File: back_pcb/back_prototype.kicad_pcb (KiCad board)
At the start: 2 copper layers, 40 x 100 mm, 74 parts, among them P1 EXPANSION_LEFT, P2 EXPANSION_BOTTOM, P3 EXPANSION_TOP, P4 USB_A, P5 AUDIO_CONN, P6 ATMEGA_HEADER, P7 EXPANSION_BOTTOM2, P8 JST, P9 USB_A, Q1 IRLML6401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

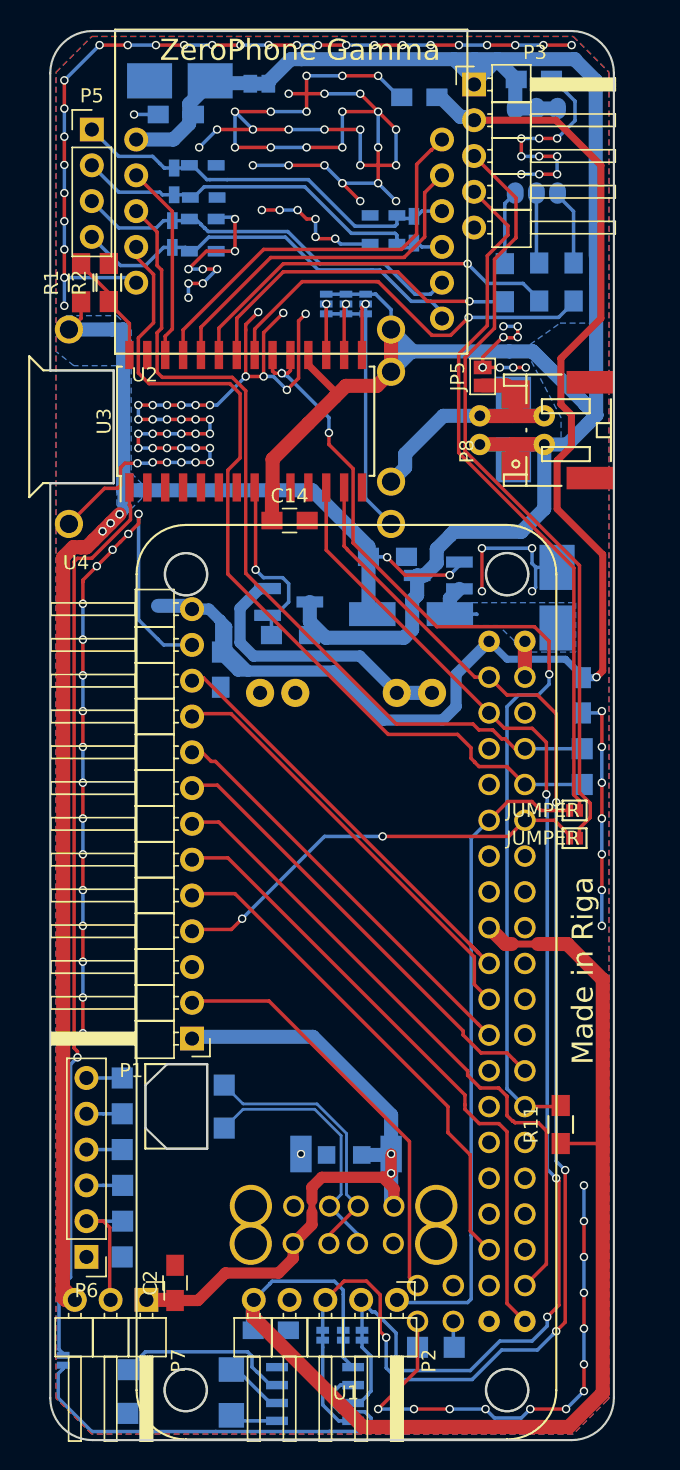
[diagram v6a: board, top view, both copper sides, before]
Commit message: Updated back board
* Added a footprint for MPU9050/9150 breakouts
* Added a FET that interrupts VBAT+ and is controlled from GPIO expander
(with a button to reset it?)
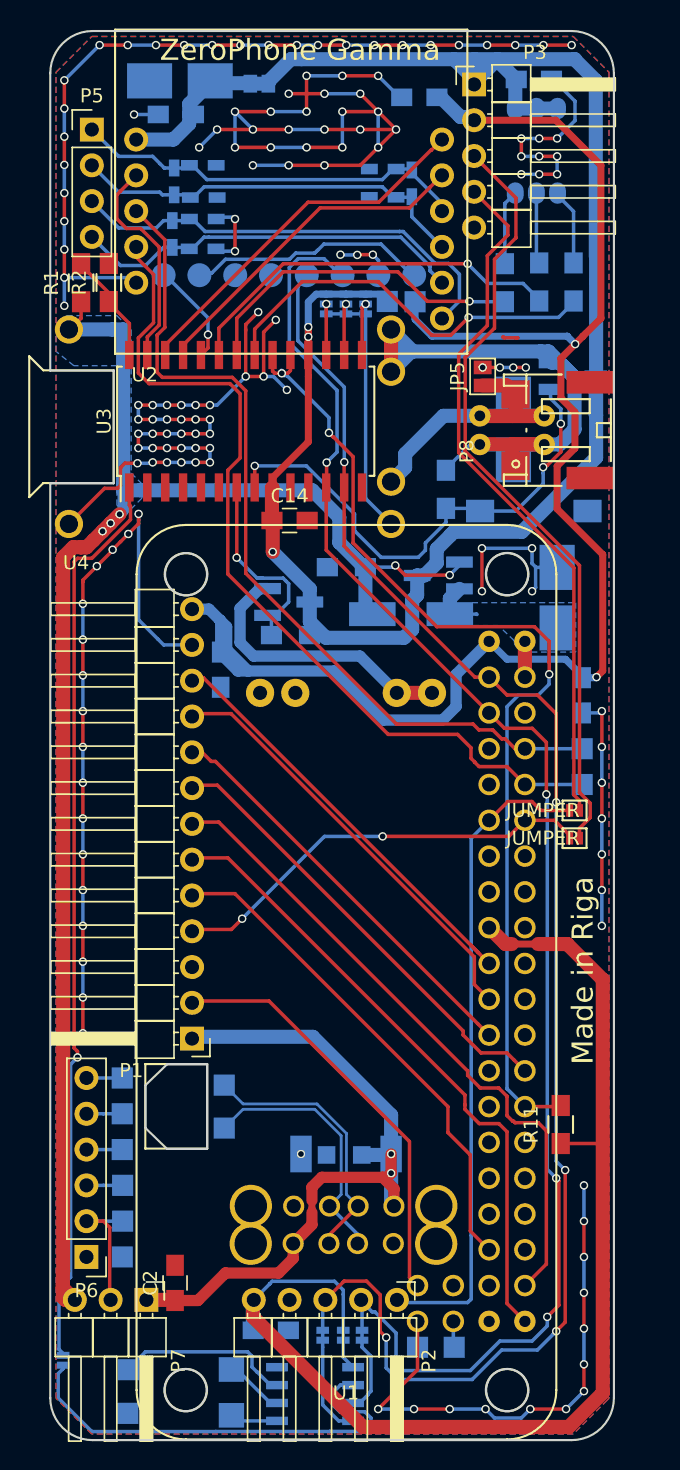
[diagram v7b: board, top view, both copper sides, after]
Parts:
- added P10: CONN_01X08, Pin_Headers:Pin_Header_Straight_1x08_Pitch2.54mm, B.Cu at (67.3, 57.3)
- added Q2: IRLML6401, TO_SOT_Packages_SMD:SOT-23_Handsoldering, B.Cu at (78.6, 64.5)
- added R4: 10K, Resistors_SMD:R_0805_HandSoldering, B.Cu at (69.6, 72.5)
- added SW1: SW_PUSH, footprints:SW_SPST_EVQPE1, B.Cu at (75.8, 74.1)
- added W5: 3V3, Measurement_Points:Measurement_Point_Square-SMD-Pad_Small, B.Cu at (67.4, 59.2)
- added W7: VBAT, Measurement_Points:Measurement_Point_Square-SMD-Pad_Small, B.Cu at (65.4, 59.2)
- moved C16 3.32 mm to (65.1, 51.8)
- moved C17 3.30 mm to (67.2, 50.8)
- moved C18 3.29 mm to (65.1, 49.8)
- moved R3 3.01 mm to (62.5, 78.0), turned to 180 degrees
- moved C19 0.17 mm to (52.3, 55.5)
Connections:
- C19 pad 2: SPK- -> SPK+
- C20 pad 1: SPK- -> SPK+
- C20 pad 2: SPK+ -> SPK-
- C21 pad 1: SPK+ -> SPK-
- C3 pad 1: +BATT -> BATT+
- P5 pad 3: SPK+ -> SPK-
- P5 pad 4: SPK- -> SPK+
- P8 pad 1: +BATT -> BATT+
- U3 pad 24: SIM800_DTR -> IMU_INT
- U3 pad 25: SIM800_RING -> SIM800_DTR
- U3 pad 26: SIM800_RST -> SIM800_RING
- U3 pad 27: (no net) -> SIM800_RST
- U3 pad 7: (no net) -> DCDC_EN
- U3 pad 8: DCDC_EN -> VBAT_EN
- U4 pad 3: +BATT -> BATT+
- U4 pad 4: +BATT -> BATT+
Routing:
- net BATT+: track 0.00 -> 47.1 mm
- net +BATT: track 179.4 -> 142.0 mm, vias 0 -> 3
- net VBAT_EN: track 0.00 -> 36.3 mm, vias 0 -> 3
- net GND: track 394.8 -> 359.4 mm, vias 172 -> 152
- net SCL: track 94.4 -> 116.3 mm, vias 3 -> 4
- net Net-(P10-Pad1): track 0.00 -> 17.1 mm
- net SDA: track 103.1 -> 119.7 mm, vias 4 -> 5
- net +3V3: track 186.3 -> 197.5 mm, vias 1 -> 2
- net IMU_INT: track 0.00 -> 7.31 mm, vias 0 -> 1
- net SPK-: track 29.4 -> 32.5 mm
- net SIM800_RING: track 28.6 -> 26.4 mm
- net SIM800_RST: track 14.0 -> 15.5 mm
- net SIM800_DTR: track 25.4 -> 24.1 mm
- net DCDC_EN: track 13.3 -> 14.6 mm
- net VDD: track 114.4 -> 115.5 mm
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- removed copper zone on B.Cu, net +BATT

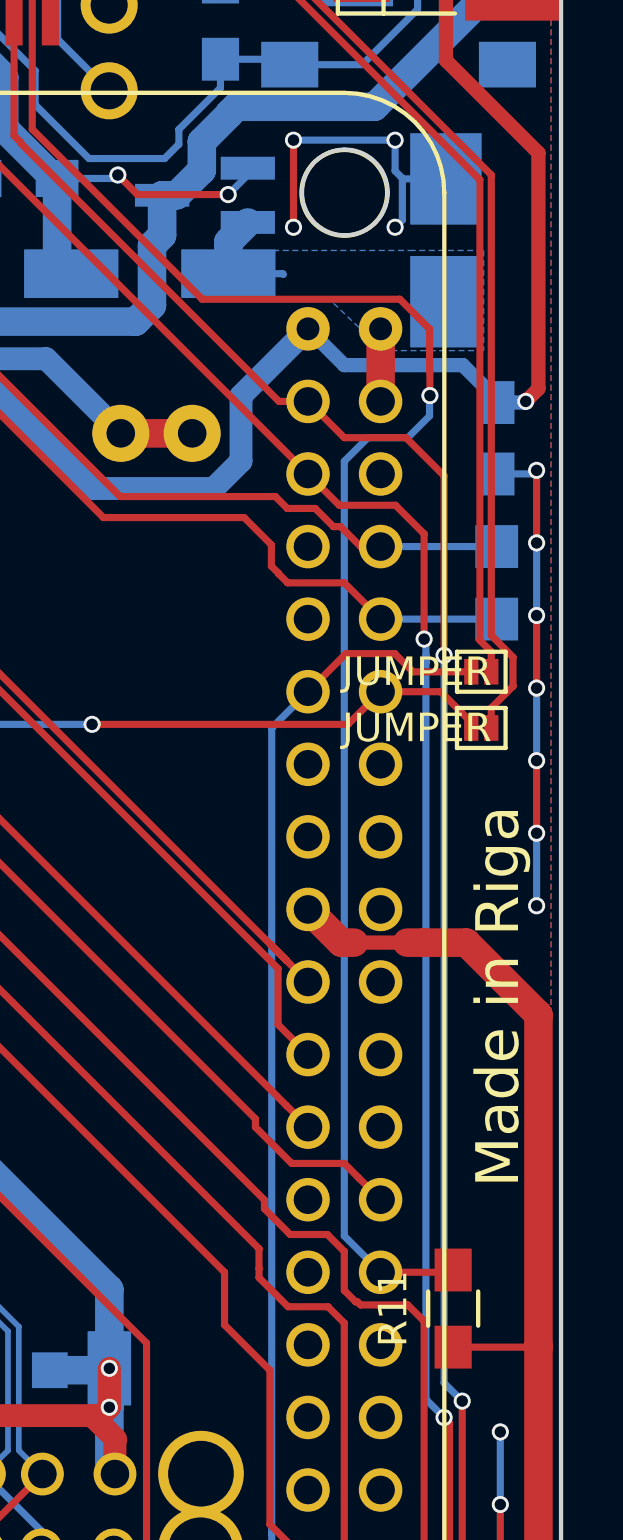
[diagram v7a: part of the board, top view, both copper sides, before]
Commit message: Started using GPIO4 for IR TX
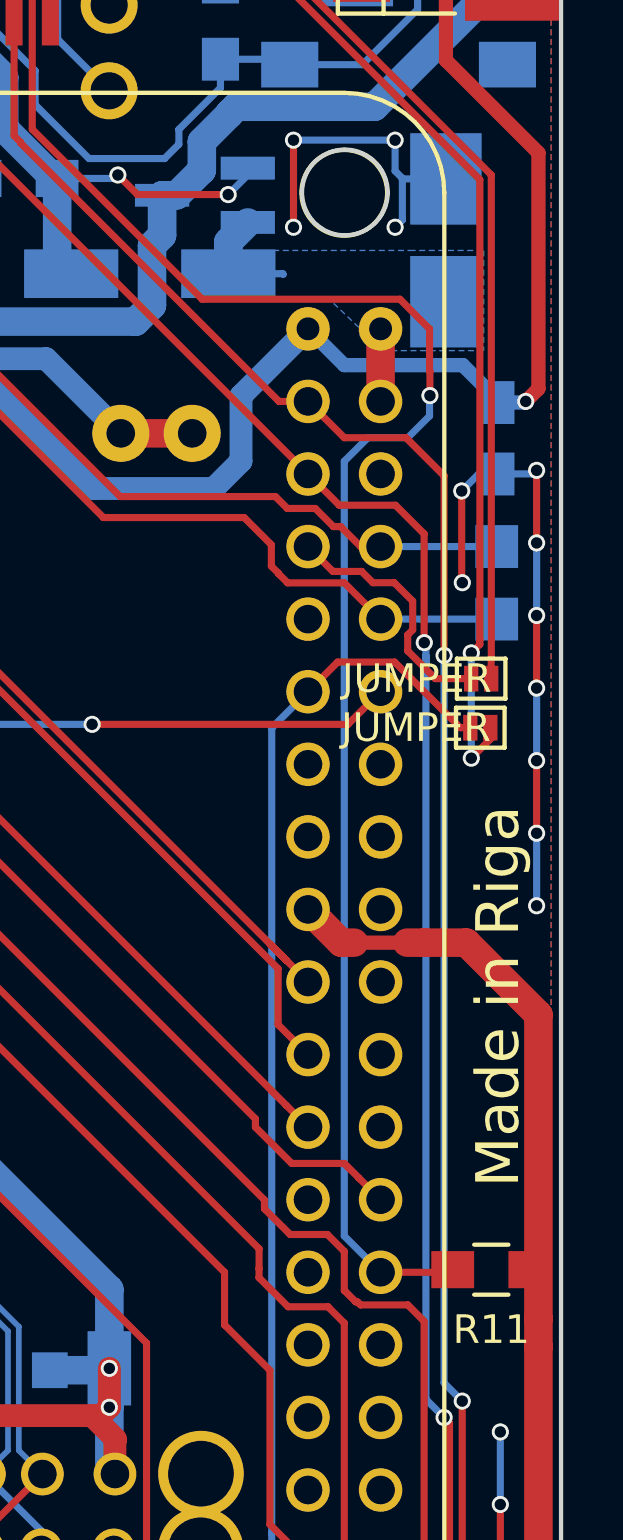
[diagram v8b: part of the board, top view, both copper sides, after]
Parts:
- moved JP11 1.96 mm to (79.0, 97.3)
- moved R11 1.91 mm to (79.1, 116.2), turned to 180 degrees
- moved JP12 1.73 mm to (79.1, 95.6)
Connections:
- JP12 pad 1: LH_GPIO_4 -> Net-(JP12-Pad1)
- U1 pad 7: (no net) -> Net-(JP12-Pad1)
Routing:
- net Net-(JP12-Pad1): track 0.00 -> 8.89 mm
- net IR_RX: track 49.9 -> 54.2 mm, vias 0 -> 2
- net LH_GPIO_4: track 30.6 -> 26.8 mm
- net GND: track 359.4 -> 362.8 mm, vias 152 -> 154
- net IR_TX: track 55.1 -> 52.8 mm
- net (no net): track 0.00 -> 1.24 mm
- net +3V3: track 197.5 -> 196.4 mm
- net BH_GPIO_1: track 46.5 -> 47.0 mm
